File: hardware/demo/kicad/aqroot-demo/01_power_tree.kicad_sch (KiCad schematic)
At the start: 138 parts, among them J3 USB_C_Receptacle_USB2.0_16P, J4 JST-PH-2 BATTERY, Q2 NTMD4820N, Q3 NTMD4820N, Q4 BSS138, Q5 AO3401A, Q6 BSS138, Q7 BSS138, Q8 BSS138, Q9 BSS138, SW9 SW_SPDT, U10 USBLC6-2SC6, U11 BQ25185, U12 TPS63020, U13 TPS61023, U14 MAX17048, U18 LTC4368-1, U19 TLV7032, U20 TPS22950C, U21 TPS61023, U22 TPS22950C

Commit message: demo: the fabrication package EXISTS for the first time, and the review found three things the gate could not see -- a BOM that quoted forty-six test points, one part number on two land patterns, and a schematic-parity check that had never been asked (D-613)
NO COPPER CHANGED. The authoritative board is byte-identical at c8e421aa...,
the ledger reads 57 open edges row for row, ratsnest 73, protected copper
15 nets / 393 objects IDENTICAL. Two files changed under kicad/: eleven lines
removed from one schematic sheet.

THE PACKAGE. export_fab_package.py produces all 28 artifacts in one command
from the authoritative board -- thirteen Gerbers plus KiCad's own .gbrjob,
separate PTH/NPTH Excellon at ABSOLUTE origin, drill maps and report, two
position files, five BOM views, F.Fab/B.Fab assembly PDFs with D-612's sixteen
DNP parts crossed out -- into hardware/demo/fab/. It is REPRODUCIBLE: KiCad
stamps a date into Gerber and Excellon headers, so MANIFEST.json also carries a
NORMALISED sha256 with those lines removed, stable run to run, for 24 of the 28;
the four PDFs embed a date inside the document and are recorded
deterministic: false rather than quietly excluded from the claim.

THE REVIEW MEASURES CONSEQUENCES, NOT FLAGS (checks/fab_package_contract.py).
FAB4 is not "a drill file exists": both Excellon files are parsed into board
coordinates and matched against pcbnew's vias and pad drills -- 802 holes on the
board, 802 in the files, ZERO displaced, to the micron, the resolution the file
is written at. FAB2 proves the committed board is BYTE-IDENTICAL after
--refill-zones --save-board, which matters because Gerber export does NOT
refill; a stale stored fill would ship copper no check here has ever inspected.
FAB1-FAB6 and FAB8 PASS; FAB7 FAILS and is the blocker.

FINDING 1 -- the BOM asked a supplier to quote forty-six test points. Every one
of the schematic's 310 symbols says (in_bom yes); 46 are TestPoint -- a pad --
and the BOARD already carried KiCad's exclude-fr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
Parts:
- C26: LCSC C344022 -> (none)
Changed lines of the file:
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@@
-			)
-		)
-		(property "LCSC" "C344022"
-			(at 266.7 105.41 0)
-			(hide yes)
-			(show_name no)
-			(do_not_autoplace no)
-			(effects
-				(font
-					(size 1.27 1.27)
-				)
 			)
 		)

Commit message: demo: the BOM is THREE QUARTERS orderable -- 122 part identities grafted from prior CTO audits, every one re-read off the PART instead of the line, and four gates that had never been run (D-614)
NO COPPER CHANGED.  The authoritative board is byte-identical at
c8e421aa50144fe396aedb5e226aaabeb815bd69ffaf6e04f549ded43831d103 and 26 of the
package's 28 artifacts are normalised-sha-identical to D-613's; the two that
moved are the two BOM views.

FAB7 coverage 25.9% -> 75.3%, orderable references 64 -> 186 of 247.
36 BOM lines / 122 references gained Manufacturer / MPN / LCSC -- 487 properties
across nine schematic sheets, replayable to byte-identical sheets.

Four things the mechanical answer would have got wrong: a REJECTED audit row's
JLC Manufacturer column names the match that was THROWN OUT (16 of 31 grafts);
the rating belongs to the PART, not the line; the designator is not the
identity; and the beta-dm 0 ohm current gate had never been run on five of the
Demo's eight links.

Two defects in the instruments fixed: the value parser could not read 15mR, and
MANIFEST.json hashed only the ROOT schematic sheet while nine child sheets
changed.

Re-proved on this tree: verify_promotion.py 14/14, FAB1-FAB6 + FAB8 PASS,
POP1-POP4, P1-P4, protected copper 15 nets / 393 objects IDENTICAL.
FAB7 still FAILS and is partitioned: 8 lines / 16 parts TUNE, 26 lines /
45 parts genuinely open.

Co-Authored-By: Claude Opus 5 <noreply@anthropic.com>
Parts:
- C20: LCSC (none) -> C354262; MPN (none) -> CC0805KKX7R8BB475; Manufacturer (none) -> YAGEO; Note_Sourcing (none) -> SOURCING D-614. EXACT_PRIOR from the beta-dm audit line '4.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
- C23, C25, C58, C59, C62, C63, C67: LCSC (none) -> C106858; MPN (none) -> CC0603KRX7R8BB105; Manufacturer (none) -> YAGEO; Note_Sourcing (none) -> SOURCING D-614. EXACT_PRIOR from the beta-dm audit line '1u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
- C26, C27: LCSC (none) -> C77093; MPN (none) -> GRM31CR71E106KA12L; Manufacturer (none) -> Murata Electronics; Note_Sourcing (none) -> SOURCING D-614. EXACT_PRIOR from the beta-dm audit line '10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
- C28, C36, C60, C61, C68: LCSC (none) -> C14663; MPN (none) -> CC0603KRX7R9BB104; Manufacturer (none) -> YAGEO; Note_Sourcing (none) -> SOURCING D-614. EXACT_PRIOR from the beta-dm audit line '10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
- C29, C30, C31, C32: LCSC (none) -> C22392398; MPN (none) -> TCC1206X7R226K160HT; Manufacturer (none) -> CCTC; Note_Sourcing (none) -> SOURCING D-614. EXACT_PRIOR from the beta-dm audit line '22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
- C33, C64: LCSC (none) -> C326595; MPN (none) -> CC0805KKX7R7BB106; Manufacturer (none) -> YAGEO; Note_Sourcing (none) -> SOURCING D-614. EXACT_PRIOR from the beta-dm audit line '10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
- R100, R102, R103, R131, R43, R81, R98: LCSC (none) -> C25803; MPN (none) -> 0603WAF1003T5E; Manufacturer (none) -> UNI-ROYAL(Uniroyal Elec); Note_Sourcing (none) -> SOURCING D-614. EXACT_PRIOR from the beta-dm audit line '10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
- R106: LCSC (none) -> C21189; MPN (none) -> 0603WAF0000T5E; Manufacturer (none) -> UNI-ROYAL(Uniroyal Elec); Note_Sourcing (none) -> SOURCING D-614. CONTAINED_PRIOR from the beta-dm audit line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
- R30, R31: LCSC (none) -> C23186; MPN (none) -> 0603WAF5101T5E; Manufacturer (none) -> UNI-ROYAL(Uniroyal Elec); Note_Sourcing (none) -> SOURCING D-614. EXACT_PRIOR from the beta-dm audit line '5.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
- R32, R35, R42: LCSC (none) -> C21189; MPN (none) -> 0603WAF0000T5E; Manufacturer (none) -> UNI-ROYAL(Uniroyal Elec); Note_Sourcing (none) -> SOURCING D-614. EXACT_PRIOR from the beta-dm audit line '0R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
- R33, R34: LCSC (none) -> C23345; MPN (none) -> 0603WAF220JT5E; Manufacturer (none) -> UNI-ROYAL(Uniroyal Elec); Note_Sourcing (none) -> SOURCING D-614. EXACT_PRIOR from the beta-dm audit line '22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
- R36: LCSC (none) -> C25810; MPN (none) -> 0603WAF1802T5E; Manufacturer (none) -> UNI-ROYAL(Uniroyal Elec); Note_Sourcing (none) -> SOURCING D-614. EXACT_PRIOR from the beta-dm audit line '18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
- R37: LCSC (none) -> C21190; MPN (none) -> 0603WAF1001T5E; Manufacturer (none) -> UNI-ROYAL(Uniroyal Elec); Note_Sourcing (none) -> SOURCING D-614. EXACT_PRIOR from the beta-dm audit line '1k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
- R38, R83: LCSC (none) -> C25804; MPN (none) -> 0603WAF1002T5E; Manufacturer (none) -> UNI-ROYAL(Uniroyal Elec); Note_Sourcing (none) -> SOURCING D-614. EXACT_PRIOR from the beta-dm audit line '10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
- R39, R41, R80, R82, R94, R96: LCSC (none) -> C22935; MPN (none) -> 0603WAF1004T5E; Manufacturer (none) -> UNI-ROYAL(Uniroyal Elec); Note_Sourcing (none) -> SOURCING D-614. EXACT_PRIOR from the beta-dm audit line '1M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
- R40: LCSC (none) -> C22827; MPN (none) -> 0603WAF1803T5E; Manufacturer (none) -> UNI-ROYAL(Uniroyal Elec); Note_Sourcing (none) -> SOURCING D-614. EXACT_PRIOR from the beta-dm audit line '18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
- R84: LCSC (none) -> C22775; MPN (none) -> 0603WAF1000T5E; Manufacturer (none) -> UNI-ROYAL(Uniroyal Elec); Note_Sourcing (none) -> SOURCING D-614. CONTAINED_PRIOR from the beta-dm audit line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

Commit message: demo: the BOM is 100% ORDERABLE and the safety part was ordered in the WRONG PACKAGE -- 61 identities ruled against a live distributor record, and a screen that asks the C26 question of every line at once (D-615)
D-614 named this task and named what stopped it: D-096 binds -- a part number
configured from an ordering scheme is a hypothesis until a distributor record
confirms lifecycle and stock, and that session had none to read.  This one read
the JLCPCB catalogue 225 times and KEPT every answer, each stamped with the UTC
minute it was read.

NO COPPER CHANGED.  The authoritative board is byte-identical at
c8e421aa50144fe396aedb5e226aaabeb815bd69ffaf6e04f549ded43831d103.

FAB7 IS CLOSED.  Coverage 75.3% -> 100.0%, orderable 186 -> 247 of 247,
needs_a_sourcing_decision ZERO lines, and fab_package_contract.py reads
FAB1-FAB8 PASS for the first time.

THE FINDING.  screen_part_land_parity.py asks D-613's C26 question of every
sourced line at once against the catalogue's own package field: 119 lines carry
a code, 75 are comparable, 74 MATCH and U18 did not.  The land is MSOP-10; the
BOM ordered LTC4368IDD-1#PBF, and DD is DFN-10-EP(3x3) -- against D-099, which
locked LTC4368IMS-1#PBF under FBV2-PWR-002's "no bottom-terminated parts" on
the single most safety-critical component.  The cached library symbol AND the
project .kicad_sym both still carried it, with a Package field describing a DFN
beside a Footprint field already reading MSOP-10.  Corrected to
LTC4368IMS-1#TRPBF, LCSC C688401 -- the tape-and-reel order code of the
identical device, D-210's precedent, not an electrical change.

Three things the obvious answer would have got wrong: R69 is 1.87 ohm and its
part is 0603WAF187KT5E while 0603WAF1873T5E is 187 kOhm; R95's node over-bound
UNDERSTATES its dissipation because a reversed cell adds in series (154 mW vs
54 mW); and R24/C12's Value strings are looser than their own symbol notes.
NET_MAX_DC grew 17 -> 48 established nodes to give the new dissipation gate
nu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
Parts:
- C57: LCSC (none) -> C53987; MPN (none) -> 0603B472K500NT; Manufacturer (none) -> FH (Guangdong Fenghua Advanced Tech); Note_Sourcing (none) -> SOURCING D-615 LIVE_RECORD. JLCPCB record read 2026-09-05T0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
- C65, C66: LCSC (none) -> C907991; MPN (none) -> GRM21BZ71A226ME15L; Manufacturer (none) -> Murata Electronics; Note_Sourcing (none) -> SOURCING D-615 LIVE_RECORD. JLCPCB record read 2026-09-05T0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
- R101: LCSC (none) -> C4088673; MPN (none) -> ERJ-PA3F1651V; Manufacturer (none) -> PANASONIC; Note_Sourcing (none) -> SOURCING D-615 LIVE_RECORD. JLCPCB record read 2026-09-05T0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
- R104: LCSC (none) -> C22807; MPN (none) -> 0603WAF1503T5E; Manufacturer (none) -> UNI-ROYAL(Uniroyal Elec); Note_Sourcing (none) -> SOURCING D-615 LIVE_RECORD. JLCPCB record read 2026-09-05T0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
- R105: LCSC (none) -> C22961; MPN (none) -> 0603WAF2203T5E; Manufacturer (none) -> UNI-ROYAL(Uniroyal Elec); Note_Sourcing (none) -> SOURCING D-615 LIVE_RECORD. JLCPCB record read 2026-09-05T0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
- R75: LCSC (none) -> C2073490; MPN (none) -> CRA2512-FZ-R015ELF; Manufacturer (none) -> BOURNS; Note_Sourcing (none) -> SOURCING D-615 LIVE_RECORD. JLCPCB record read 2026-09-05T0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
- R76: LCSC (none) -> C31850; MPN (none) -> 0603WAF2202T5E; Manufacturer (none) -> UNI-ROYAL(Uniroyal Elec); Note_Sourcing (none) -> SOURCING D-615 LIVE_RECORD. JLCPCB record read 2026-09-05T0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
- R77, R91: LCSC (none) -> C482835; MPN (none) -> RC0603FR-073M65L; Manufacturer (none) -> YAGEO; Note_Sourcing (none) -> SOURCING D-615 LIVE_RECORD. JLCPCB record read 2026-09-05T0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
- R78: LCSC (none) -> C185327; MPN (none) -> RC0603FR-07442KL; Manufacturer (none) -> YAGEO; Note_Sourcing (none) -> SOURCING D-615 LIVE_RECORD. JLCPCB record read 2026-09-05T0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
- R79: LCSC (none) -> C23192; MPN (none) -> 0603WAF5103T5E; Manufacturer (none) -> UNI-ROYAL(Uniroyal Elec); Note_Sourcing (none) -> SOURCING D-615 LIVE_RECORD. JLCPCB record read 2026-09-05T0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
- R85, R86, R87, R88, R89, R90: LCSC (none) -> C137747; MPN (none) -> RC0603FR-072M2L; Manufacturer (none) -> YAGEO; Note_Sourcing (none) -> SOURCING D-615 LIVE_RECORD. JLCPCB record read 2026-09-05T0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
- R92: LCSC (none) -> C2115863; MPN (none) -> MCT06030C1304FP500; Manufacturer (none) -> Vishay Intertech; Note_Sourcing (none) -> SOURCING D-615 LIVE_RECORD. JLCPCB record read 2026-09-05T0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
- R95: LCSC (none) -> C4220370; MPN (none) -> ERJ-P08F5600V; Manufacturer (none) -> PANASONIC; Note_Sourcing (none) -> SOURCING D-615 LIVE_RECORD. JLCPCB record read 2026-09-05T0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
- R97: LCSC (none) -> C22843; MPN (none) -> 0603WAF1501T5E; Manufacturer (none) -> UNI-ROYAL(Uniroyal Elec); Note_Sourcing (none) -> SOURCING D-615 LIVE_RECORD. JLCPCB record read 2026-09-05T0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
- R99: LCSC (none) -> C2079739; MPN (none) -> CRCW0603732KFKEA; Manufacturer (none) -> Vishay Intertech; Note_Sourcing (none) -> SOURCING D-615 LIVE_RECORD. JLCPCB record read 2026-09-05T0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
- U18: LCSC C688397 -> C688401; MPN LTC4368IDD-1#PBF -> LTC4368IMS-1#TRPBF; Note2 SOURCING 2026-08-23 (FBV2-S2-002) (B-71) - FIRST-BUILD BLOC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 -> SUPERSEDED BY D-615 -- the part this note prices is the DD 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; Note_Sourcing (none) -> SOURCING D-615 PACKAGE CORRECTION. The board land is Packag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

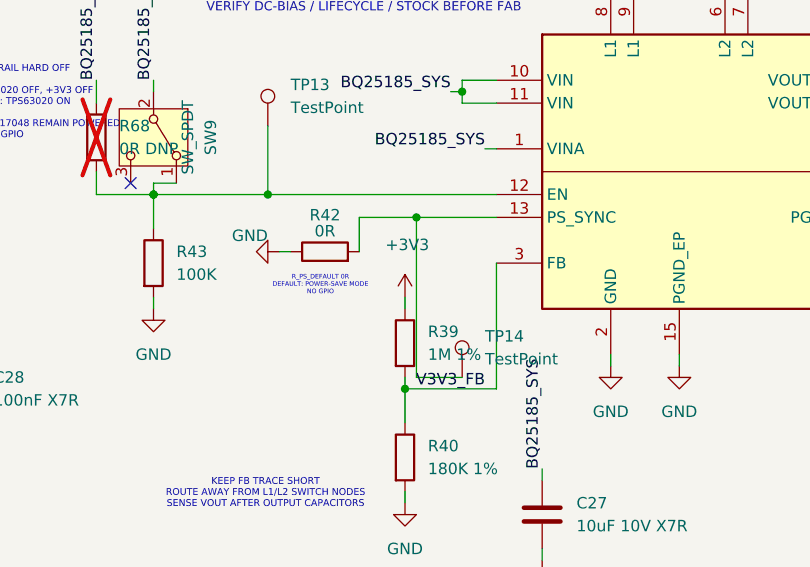
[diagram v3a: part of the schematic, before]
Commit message: demo: D-712 -- THE U2 CHANNEL SWAP IS PROMOTED AND /BQ25185_STAT1 IS CLOSED, AND THE TPS63020's PS/SYNC STRAP COMES HOME FROM FIFTY MILLIMETRES AWAY: 15 -> 13 RETAINED OPEN EDGES.
COPPER PROMOTED.  Authority 4414da31 -> 2e8ef9ed; 15 -> 13 retained open
edges over 9 nets.  hardware/beta-v2 UNTOUCHED.

1. D-711's U2 CHANNEL SWAP, SPENT.  P05 <-> P17 and P06 <-> P16 on the
   PCAL9535A, schematic and PCB together.  /BQ25185_STAT1 and /BQ25185_STAT2
   were landed on U2's WEST column with their partners at x 59..70, and
   /SX1262_DIO1 and /TOUCH_INT_N on its EAST column with their partners at
   x 3 and x 22; all four crossed the package.  The netlist diff is exactly
   four nets plus GND, ERC drops 4 (the two removed parts' library links) and
   gains nothing, and /BQ25185_STAT1 now ROUTES: 1 -> 0 open edges.
   /TOUCH_INT_N was evicted whole and comes back closed.

2. THE PS/SYNC STRAP.  R42 is a 0R tying U12.13 (PS/SYNC on the TPS63020) to
   GND and it sat at (16.665, 120.335) -- FIFTY MILLIMETRES from the pin --
   with TP14 on the way, hauling 33 B.Cu objects across the board.  Its last
   two segments lay in the C24/C26 gate, which D-649 measured as a SINGLE-FILE
   corridor the /01_POWER_TREE/BQ25185_SYS pour and that net cannot share --
   which is why C26.2, a 10 uF bulk capacitor on the system rail, was an
   ISLAND.  A 0R to GND and a tie to GND are the same circuit, so U12.13 is
   tied to U12.15, U12's own thermal ground pad, 0.610 mm away, and R42 and
   TP14 come off the board.  BQ25185_SYS 5 -> 4 open edges, and a switching
   converter's mode pin stops being a 50 mm antenna.

3. TP7 OUT OF THE POWER POUR.  /BQ25185_STAT2's test point sat at
   (62.750, 98.500), inside the B.Cu BQ25185_SYS pour, in the 0.4 mm neck that
   is the rail's only north-south conductor.  Every STAT2 re-route through it
   severed the pour.  TP7 moves to (57.500, 97.500), clear of the pour.

4. THE SYS SPINE IS RESERVED DURING THE RUN.  evidence/d712-guard-spine.json
   sample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
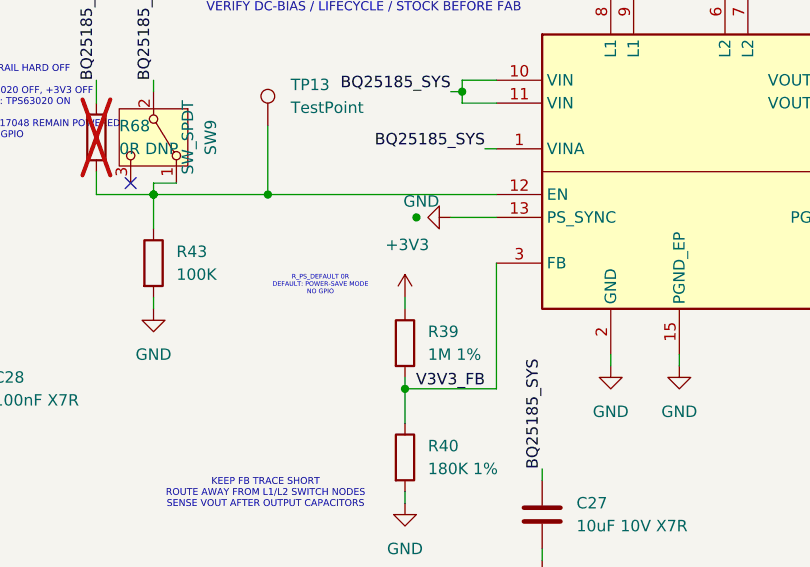
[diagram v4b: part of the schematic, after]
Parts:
- removed R42: 0R, Resistor_SMD:R_0603_1608Metric, symbol Device:R
- removed TP14: TestPoint, TestPoint:TestPoint_Pad_D1.0mm, symbol Connector:TestPoint
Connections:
- net GND: now also U12.13 (PS_SYNC)

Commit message: demo: D-742 -- the owner decision on U11.3 is SPENT, and reading the datasheet to spend it found that this board's charger status decode was INVERTED on STAT1.
The owner approved (2026-09-17) leaving /BQ25185_STAT2's U11.3 unconnected.  routing_ledger.py now carries APPROVED_UNROUTED, deliberately NOT folded into APPROVED_NC: a J5 NC contact carries no net and is simply not counted, whereas U11.3 carries a real net on a fitted part and is genuinely unrouted.  Folding it in would have deleted the board's record of why the pin is bare AND made neck_contract N2 vacuous, because U11.3 is the only pad N2 compares on this board.  So nets[] keeps telling the copper truth -- retained_open_edges stays 1 -- and the governance verdict is published beside it: approved_unrouted_edges 1, unapproved_open_edges 0.  The declaration is re-proved against the board every run (pad exists, part fitted, net matches, still stranded, R128 and TP7 still fitted) and four non-vacuity controls show it FAILS when any of those stops being true.

Then the datasheet was read, which nobody in this programme had done since 2026-08, and the independent review's pre-fab item "validate STAT1/STAT2 decoding against the current TI truth table" turned out not to be a formality.  THE DECODE THIS BOARD CARRIED WAS INVERTED ON STAT1.  R127/R128's schematic notes and D-170 all said "STAT1 LOW = charging; STAT1 HIGH + STAT2 LOW = fault", citing a "SLUSF65A Table 7-2" that is not a status table.  SLUSF65B section 6.3.10 Table 6-2 says the opposite on both rows: STAT1 LOW is a FAULT, STAT1 HIGH with STAT2 LOW is CHARGING.  The datasheet confirms its own table twice more (section 6.3.7.1's VIN_OVP row, and the flow diagram's "STAT1 and STAT2 to 1" for Charge Done), and its revision history shows TI never changed the table -- this was a reading error made in FBV2-S1-008 and copied ever since.  POWER_FAULT_STATE_TABLE.md had it right the whole time and nothing compared the two.

The correction makes the owner decisi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
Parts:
- U13: Note (none) -> D-742 (2026-09-18) RECORDS TWO THINGS ABOUT THIS PART THAT 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
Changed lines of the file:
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@@
+			)
+		)
+		(property "Note" "D-742 (2026-09-18) RECORDS TWO THINGS ABOUT THIS PART THAT FIRMWARE AND ANY REVIEWER MUST READ TOGETHER. (1) PIN 3 STAT2 IS INTENTIONALLY UNCONNECTED ON AQROOT DEMO - OWNER DECISION, 2026-09-17. The /BQ25185_STAT2 net is retained and fully routed on its other three contacts (R128 10k pull-up to +3V3, TP7 test point, and U2.19 = PCAL9535A U2 P16), but U11.3 itself has no escape. MEASURED REASON (D-734, re-measured D-741): U11.2's BAT_PROTECTED_P escape must leave on its own land centreline y=78.200 mm because 0.200 mm of pad clearance to U11.1's SYS land at y>=78.500 mm pins it there; D-269's 0.300 mm battery-conductor clearance then caps STAT2's escape at y<=77.800 mm, and U11.4's GND land at y<=77.500 mm floors it at y>=77.700 mm. The window is 0.100 mm against this board's published 0.200 mm minimum track width. It does not move with U11's position and it does not move with rotation, because BAT is pin 2 and STAT2 is pin 3 in every DLH0010A. A via-in-pad escape is impossible too: the smallest barrel this board's own floors permit is 0.450 mm across and the land is 0.750 x 0.200 mm. SLUSF65B Table 4-1 states that STAT1 and STAT2 may be left floating if unused, so this is electrically inert. R128 and TP7 are RETAINED so the signal stays probeable and bodgeable for bench bring-up and a Rev-B respin; DO NOT DEPOPULATE THEM. (2) THE CHARGE-STATE DECODE THIS BOARD CARRIED WAS INVERTED ON STAT1, AND D-742 CORRECTED IT. The authority is SLUSF65B (August 2026) section 6.3.10 Table 6-2; the 'Table 7-2' the old notes cited is not a status table at all. THE CORRECT TABLE: STAT1 HIGH + STAT2 HIGH = charge completed, sleep, or charge disabled (including VBAT > VRCH); STAT1 HIGH + STAT2 LOW = NORMAL CHARGING IN PROGRESS; STAT1 LOW + STAT2 HIGH = RECOVERABLE FAULT (VIN_OVP, TS HOT, TS COLD, TSHUT, system short protection); STAT1 LOW + STAT2 LOW = NON-RECOVERABLE OR LATCH-OFF FAULT (ILIM/ISET pin short, BATOCP, safety timer expired). The retired text had STAT1 LOW meaning 'charging' and STAT1 HIGH with STAT2 LOW meaning 'fault' - both rows exactly backwards. COLLAPSED ONTO STAT1 ALONE, WHICH IS ALL THIS REVISION HAS: STAT1 LOW = FAULT, DIRECTLY OBSERVED (recoverable versus non-recoverable is not distinguishable); STAT1 HIGH = NOT FAULTED, and ambiguous between charging and charge-complete / sleep / disabled. THE DEMO KEEPS FAULT DETECTION AND LOSES THE CHARGING-VERSUS-COMPLETE DISTINCTION - the opposite way round from what D-734 and the owner decision assumed while working from the inverted table. Firmware must treat STAT1 LOW as a real charger fault, and must label any charging-versus-complete claim as an INFERENCE from VBUS_PRESENT and the MAX17048 voltage and state-of-charge trend. The no-battery limit cycle of section 6.3.10 toggles STAT2 while STAT1 stays HIGH, so it is not observable here either. REV-B: this needs a charger whose STAT2 pin is not adjacent to BAT, or a package with a land taller than 0.200 mm. A different U11 departure geometry alone removes only the second of the two walls and is not sufficient. PRIMARY SOURCE, IN THE REPOSITORY: hardware/demo/kicad/aqroot-demo/vendor/BQ25185/ti-bq25185-slusf65b-2026-08.pdf, sha256 c73ed7d63e6532bb05e26df30edd37c6ac2de310c1222a84a77625e15e133684."
+			(at 53.34 105.41 0)
+			(hide yes)
+			(show_name no)
+			(do_not_autoplace no)
+			(effects
+				(font
+					(size 1.27 1.27)
+				)
 			)
 		)
